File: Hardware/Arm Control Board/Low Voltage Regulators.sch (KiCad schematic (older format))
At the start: 16 parts

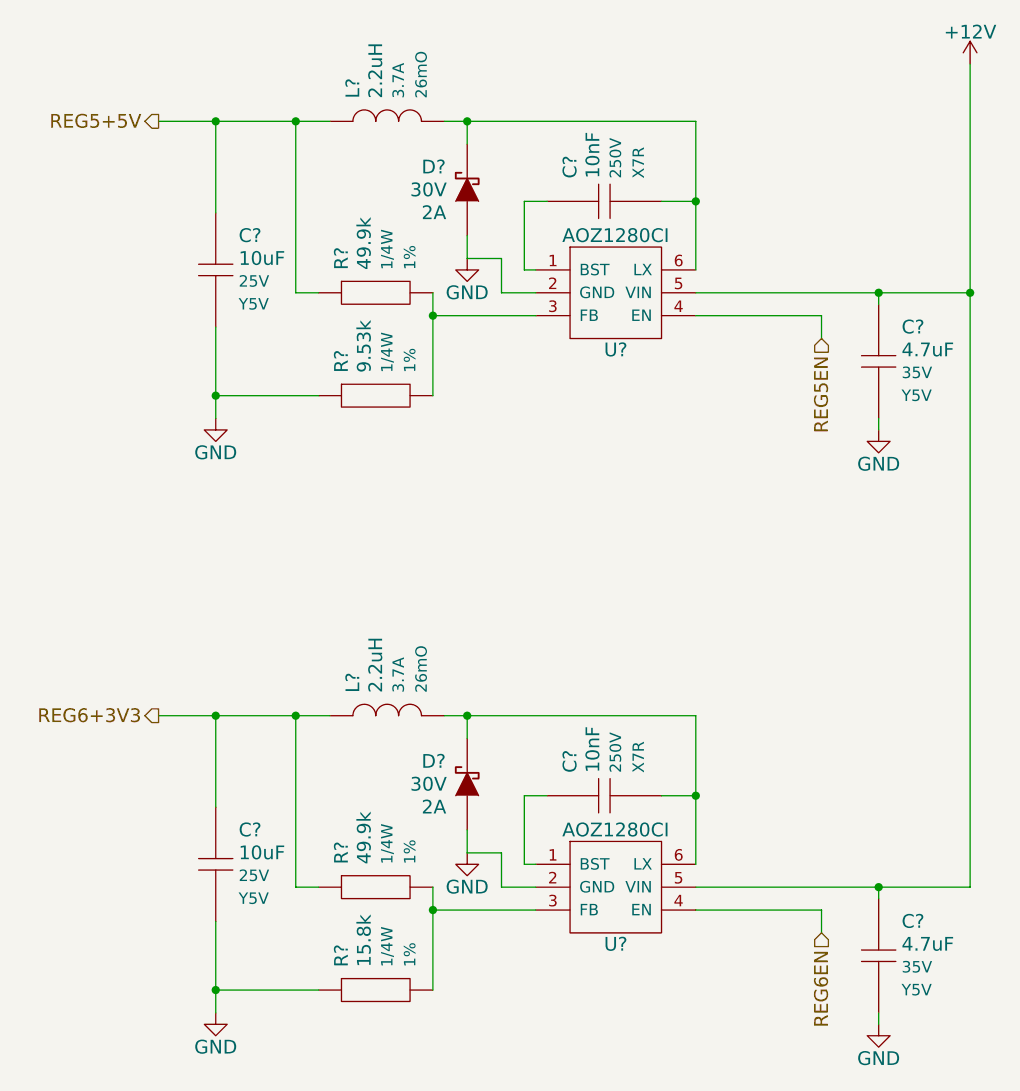
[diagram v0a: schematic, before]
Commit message: More footprints added, components annotated
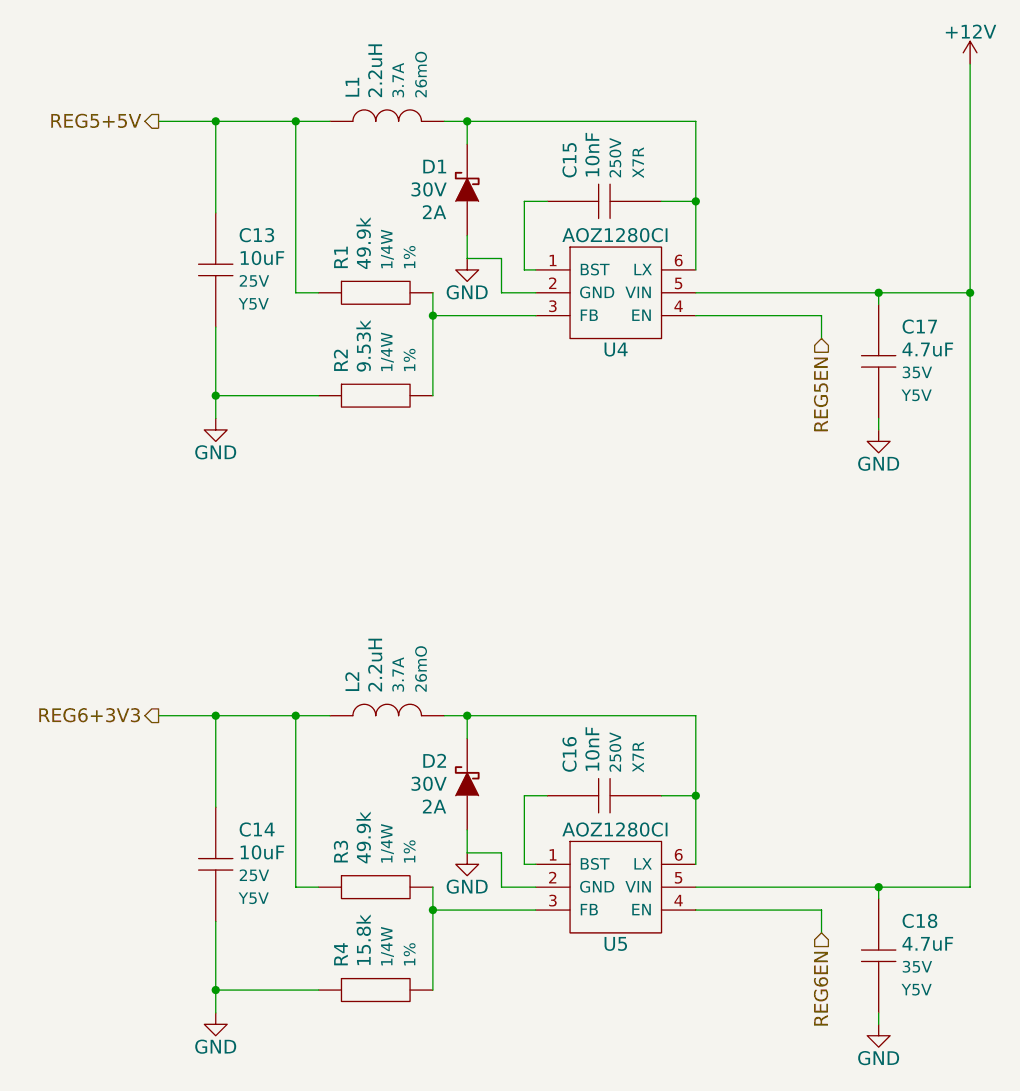
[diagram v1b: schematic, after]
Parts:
- gave numbers to parts that had none: 16
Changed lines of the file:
@@
 $EndDescr
 $Comp
-L AOZ1280CI U?
+L AOZ1280CI U5
 U 1 1 54CCFE02
 P 4200 5050
-F 0 "U?" H 4000 4700 60  0000 C CNN
+F 0 "U5" H 4000 4700 60  0000 C CNN
 F 1 "AOZ1280CI" H 4000 5200 60  0000 C CNN
 F 2 "" H 4200 5050 60  0000 C CNN
@@
 	5550 5150 4350 5150
 $Comp
-L GND #PWR?
+L GND #PWR28
 U 1 1 54CCFE12
 P 5150 5750
-F 0 "#PWR?" H 5150 5500 60  0001 C CNN
+F 0 "#PWR28" H 5150 5500 60  0001 C CNN
 F 1 "GND" H 5150 5600 60  0000 C CNN
 F 2 "" H 5150 5750 60  0000 C CNN
@@
 	2600 5150 2700 5150
 $Comp
-L DIODESCH D?
+L DIODESCH D2
 U 1 1 54CCFE3A
 P 3350 4700
-F 0 "D?" V 3450 4900 60  0000 R CNN
+F 0 "D2" V 3450 4900 60  0000 R CNN
 F 1 "DIODESCH" H 3250 5050 50  0001 C CNN
 F 2 "" H 3350 4700 60  0000 C CNN
@@
 $EndComp
 $Comp
-L GND #PWR?
+L GND #PWR24
 U 1 1 54CCFE41
 P 2250 5700
-F 0 "#PWR?" H 2250 5450 60  0001 C CNN
+F 0 "#PWR24" H 2250 5450 60  0001 C CNN
 F 1 "GND" H 2250 5550 60  0000 C CNN
 F 2 "" H 2250 5700 60  0000 C CNN
@@
 	3350 5000 3350 4900
 $Comp
-L GND #PWR?
+L GND #PWR26
 U 1 1 54CCFE56
 P 3350 5000
-F 0 "#PWR?" H 3350 4750 60  0001 C CNN
+F 0 "#PWR26" H 3350 4750 60  0001 C CNN
 F 1 "GND" H 3350 4850 60  0000 C CNN
 F 2 "" H 3350 5000 60  0000 C CNN
@@
 Connection ~ 5150 5150
 $Comp
-L Capacitor C?
+L Capacitor C14
 U 1 1 54CE875A
 P 2250 5050
-F 0 "C?" V 2100 5150 60  0000 L CNN
+F 0 "C14" V 2100 5150 60  0000 L CNN
 F 1 "10uF" V 2200 5150 60  0000 L CNN
 F 2 "Capacitors_SMD:C_1206_HandSoldering" H 2150 5050 60  0001 C CNN
@@
 $EndComp
 $Comp
-L Capacitor C?
+L Capacitor C18
 U 1 1 54CEAD10
 P 5150 5450
-F 0 "C?" V 5000 5550 60  0000 L CNN
+F 0 "C18" V 5000 5550 60  0000 L CNN
 F 1 "4.7uF" V 5100 5550 60  0000 L CNN
 F 2 "Capacitors_SMD:C_1206_HandSoldering" H 5050 5450 60  0001 C CNN
@@
 	5150 5700 5150 5750
 $Comp
-L Capacitor C?
+L Capacitor C16
 U 1 1 54CEB334
 P 3950 4750
-F 0 "C?" V 3800 4850 60  0000 L CNN
+F 0 "C16" V 3800 4850 60  0000 L CNN
 F 1 "10nF" V 3900 4850 60  0000 L CNN
 F 2 "Capacitors_SMD:C_1206_HandSoldering" H 3850 4750 60  0001 C CNN
@@
 Connection ~ 2600 4400
 $Comp
-L Inductor L?
+L Inductor L2
 U 1 1 54CEB603
 P 3000 4400
-F 0 "L?" V 2850 4500 60  0000 L CNN
+F 0 "L2" V 2850 4500 60  0000 L CNN
 F 1 "2.2uH" V 2950 4500 60  0000 L CNN
 F 2 "" H 2900 4400 60  0001 C CNN
@@
 $EndComp
 $Comp
-L Resistor R?
+L Resistor R3
 U 1 1 54CEC508
 P 2950 5150
-F 0 "R?" V 2800 5250 60  0000 L CNN
+F 0 "R3" V 2800 5250 60  0000 L CNN
 F 1 "49.9k" V 2900 5250 60  0000 L CNN
 F 2 "Resistors_SMD:R_1206_HandSoldering" H 2850 5150 60  0001 C CNN
@@
 $EndComp
 $Comp
-L Resistor R?
+L Resistor R4
 U 1 1 54CEC68A
 P 2950 5600
-F 0 "R?" V 2800 5700 60  0000 L CNN
+F 0 "R4" V 2800 5700 60  0000 L CNN
 F 1 "15.8k" V 2900 5700 60  0000 L CNN
 F 2 "Resistors_SMD:R_1206_HandSoldering" H 2850 5600 60  0001 C CNN
@@
 $EndComp
 $Comp
-L AOZ1280CI U?
+L AOZ1280CI U4
 U 1 1 54CED059
 P 4200 2450
-F 0 "U?" H 4000 2100 60  0000 C CNN
+F 0 "U4" H 4000 2100 60  0000 C CNN
 F 1 "AOZ1280CI" H 4000 2600 60  0000 C CNN
 F 2 "" H 4200 2450 60  0000 C CNN
@@
 	4350 2550 5550 2550
 $Comp
-L GND #PWR?
+L GND #PWR27
 U 1 1 54CED061
 P 5150 3150
-F 0 "#PWR?" H 5150 2900 60  0001 C CNN
+F 0 "#PWR27" H 5150 2900 60  0001 C CNN
 F 1 "GND" H 5150 3000 60  0000 C CNN
 F 2 "" H 5150 3150 60  0000 C CNN
@@
 	2600 2550 2700 2550
 $Comp
-L DIODESCH D?
+L DIODESCH D1
 U 1 1 54CED079
 P 3350 2100
-F 0 "D?" V 3450 2300 60  0000 R CNN
+F 0 "D1" V 3450 2300 60  0000 R CNN
 F 1 "DIODESCH" H 3250 2450 50  0001 C CNN
 F 2 "" H 3350 2100 60  0000 C CNN
@@
 $EndComp
 $Comp
-L GND #PWR?
+L GND #PWR23
 U 1 1 54CED07F
 P 2250 3100
-F 0 "#PWR?" H 2250 2850 60  0001 C CNN
+F 0 "#PWR23" H 2250 2850 60  0001 C CNN
 F 1 "GND" H 2250 2950 60  0000 C CNN
 F 2 "" H 2250 3100 60  0000 C CNN
@@
 	3350 2400 3350 2300
 $Comp
-L GND #PWR?
+L GND #PWR25
 U 1 1 54CED08E
 P 3350 2400
-F 0 "#PWR?" H 3350 2150 60  0001 C CNN
+F 0 "#PWR25" H 3350 2150 60  0001 C CNN
 F 1 "GND" H 3350 2250 60  0000 C CNN
 F 2 "" H 3350 2400 60  0000 C CNN
@@
 Connection ~ 5150 2550
 $Comp
-L Capacitor C?
+L Capacitor C13
 U 1 1 54CED0A8
 P 2250 2450
-F 0 "C?" V 2100 2550 60  0000 L CNN
+F 0 "C13" V 2100 2550 60  0000 L CNN
 F 1 "10uF" V 2200 2550 60  0000 L CNN
 F 2 "Capacitors_SMD:C_1206_HandSoldering" H 2150 2450 60  0001 C CNN
@@
 $EndComp
 $Comp
-L Capacitor C?
+L Capacitor C17
 U 1 1 54CED0B4
 P 5150 2850
-F 0 "C?" V 5000 2950 60  0000 L CNN
+F 0 "C17" V 5000 2950 60  0000 L CNN
 F 1 "4.7uF" V 5100 2950 60  0000 L CNN
 F 2 "Capacitors_SMD:C_1206_HandSoldering" H 5050 2850 60  0001 C CNN
@@
 	5150 3100 5150 3150
 $Comp
-L Capacitor C?
+L Capacitor C15
 U 1 1 54CED0C1
 P 3950 2150
-F 0 "C?" V 3800 2250 60  0000 L CNN
+F 0 "C15" V 3800 2250 60  0000 L CNN
 F 1 "10nF" V 3900 2250 60  0000 L CNN
 F 2 "Capacitors_SMD:C_1206_HandSoldering" H 3850 2150 60  0001 C CNN
@@
 Connection ~ 2600 1800
 $Comp
-L Inductor L?
+L Inductor L1
 U 1 1 54CED0CF
 P 3000 1800
-F 0 "L?" V 2850 1900 60  0000 L CNN
+F 0 "L1" V 2850 1900 60  0000 L CNN
 F 1 "2.2uH" V 2950 1900 60  0000 L CNN
 F 2 "" H 2900 1800 60  0001 C CNN
@@
 $EndComp
 $Comp
-L Resistor R?
+L Resistor R1
 U 1 1 54CED0DB
 P 2950 2550
-F 0 "R?" V 2800 2650 60  0000 L CNN
+F 0 "R1" V 2800 2650 60  0000 L CNN
 F 1 "49.9k" V 2900 2650 60  0000 L CNN
 F 2 "Resistors_SMD:R_1206_HandSoldering" H 2850 2550 60  0001 C CNN
@@
 $EndComp
 $Comp
-L Resistor R?
+L Resistor R2
 U 1 1 54CED0E7
 P 2950 3000
-F 0 "R?" V 2800 3100 60  0000 L CNN
+F 0 "R2" V 2800 3100 60  0000 L CNN
 F 1 "9.53k" V 2900 3100 60  0000 L CNN
 F 2 "Resistors_SMD:R_1206_HandSoldering" H 2850 3000 60  0001 C CNN
@@
 Connection ~ 5550 2550
 $Comp
-L +12V #PWR?
+L +12V #PWR29
 U 1 1 54CEDCB5
 P 5550 1550
-F 0 "#PWR?" H 5550 1400 60  0001 C CNN
+F 0 "#PWR29" H 5550 1400 60  0001 C CNN
 F 1 "+12V" H 5550 1690 60  0000 C CNN
 F 2 "" H 5550 1550 60  0000 C CNN

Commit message: Initial PCB layout
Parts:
- U4, U5: footprint (none) -> SMD_Packages:SOT-23-6
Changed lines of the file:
@@
 F 0 "U5" H 4000 4700 60  0000 C CNN
 F 1 "AOZ1280CI" H 4000 5200 60  0000 C CNN
-F 2 "" H 4200 5050 60  0000 C CNN
+F 2 "SMD_Packages:SOT-23-6" H 4200 5050 60  0001 C CNN
 F 3 "" H 4200 5050 60  0000 C CNN
 	1    4200 5050
@@
 	5550 5150 4350 5150
 $Comp
-L GND #PWR28
+L GND #PWR025
 U 1 1 54CCFE12
 P 5150 5750
-F 0 "#PWR28" H 5150 5500 60  0001 C CNN
+F 0 "#PWR025" H 5150 5500 60  0001 C CNN
 F 1 "GND" H 5150 5600 60  0000 C CNN
 F 2 "" H 5150 5750 60  0000 C CNN
@@
 $EndComp
 $Comp
-L GND #PWR24
+L GND #PWR026
 U 1 1 54CCFE41
 P 2250 5700
-F 0 "#PWR24" H 2250 5450 60  0001 C CNN
+F 0 "#PWR026" H 2250 5450 60  0001 C CNN
 F 1 "GND" H 2250 5550 60  0000 C CNN
 F 2 "" H 2250 5700 60  0000 C CNN
@@
 	3350 5000 3350 4900
 $Comp
-L GND #PWR26
+L GND #PWR027
 U 1 1 54CCFE56
 P 3350 5000
-F 0 "#PWR26" H 3350 4750 60  0001 C CNN
+F 0 "#PWR027" H 3350 4750 60  0001 C CNN
 F 1 "GND" H 3350 4850 60  0000 C CNN
 F 2 "" H 3350 5000 60  0000 C CNN
@@
 F 0 "U4" H 4000 2100 60  0000 C CNN
 F 1 "AOZ1280CI" H 4000 2600 60  0000 C CNN
-F 2 "" H 4200 2450 60  0000 C CNN
+F 2 "SMD_Packages:SOT-23-6" H 4200 2450 60  0001 C CNN
 F 3 "" H 4200 2450 60  0000 C CNN
 	1    4200 2450
@@
 	4350 2550 5550 2550
 $Comp
-L GND #PWR27
+L GND #PWR028
 U 1 1 54CED061
 P 5150 3150
-F 0 "#PWR27" H 5150 2900 60  0001 C CNN
+F 0 "#PWR028" H 5150 2900 60  0001 C CNN
 F 1 "GND" H 5150 3000 60  0000 C CNN
 F 2 "" H 5150 3150 60  0000 C CNN
@@
 $EndComp
 $Comp
-L GND #PWR23
+L GND #PWR029
 U 1 1 54CED07F
 P 2250 3100
-F 0 "#PWR23" H 2250 2850 60  0001 C CNN
+F 0 "#PWR029" H 2250 2850 60  0001 C CNN
 F 1 "GND" H 2250 2950 60  0000 C CNN
 F 2 "" H 2250 3100 60  0000 C CNN
@@
 	3350 2400 3350 2300
 $Comp
-L GND #PWR25
+L GND #PWR030
 U 1 1 54CED08E
 P 3350 2400
-F 0 "#PWR25" H 3350 2150 60  0001 C CNN
+F 0 "#PWR030" H 3350 2150 60  0001 C CNN
 F 1 "GND" H 3350 2250 60  0000 C CNN
 F 2 "" H 3350 2400 60  0000 C CNN
@@
 Connection ~ 5550 2550
 $Comp
-L +12V #PWR29
+L +12V #PWR031
 U 1 1 54CEDCB5
 P 5550 1550
-F 0 "#PWR29" H 5550 1400 60  0001 C CNN
+F 0 "#PWR031" H 5550 1400 60  0001 C CNN
 F 1 "+12V" H 5550 1690 60  0000 C CNN
 F 2 "" H 5550 1550 60  0000 C CNN

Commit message: all components have footprints assigned now
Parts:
- D1, D2: footprint (none) -> MAVRIC_footprints:Diode_MicroSMP
- L1, L2: footprint (none) -> MAVRIC_footprints:Yuden_SMD_Power_Inductor_6060
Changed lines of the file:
@@
 F 0 "D2" V 3450 4900 60  0000 R CNN
 F 1 "DIODESCH" H 3250 5050 50  0001 C CNN
-F 2 "" H 3350 4700 60  0000 C CNN
+F 2 "MAVRIC_footprints:Diode_MicroSMP" H 3350 4700 60  0001 C CNN
 F 3 "" H 3350 4700 60  0000 C CNN
 F 4 "Vishay Semiconductor" H 3350 4700 60  0001 C CNN "Manufacturer"
@@
 F 0 "L2" V 2850 4500 60  0000 L CNN
 F 1 "2.2uH" V 2950 4500 60  0000 L CNN
-F 2 "" H 2900 4400 60  0001 C CNN
+F 2 "MAVRIC_footprints:Yuden_SMD_Power_Inductor_6060" H 2900 4400 60  0001 C CNN
 F 3 "" H 3000 4500 60  0001 C CNN
 F 4 "Taiyo Yuden" H 3000 4400 60  0001 C CNN "Manufacturer"
@@
 F 0 "D1" V 3450 2300 60  0000 R CNN
 F 1 "DIODESCH" H 3250 2450 50  0001 C CNN
-F 2 "" H 3350 2100 60  0000 C CNN
+F 2 "MAVRIC_footprints:Diode_MicroSMP" H 3350 2100 60  0001 C CNN
 F 3 "" H 3350 2100 60  0000 C CNN
 F 4 "Vishay Semiconductor" H 3350 2100 60  0001 C CNN "Manufacturer"
@@
 F 0 "L1" V 2850 1900 60  0000 L CNN
 F 1 "2.2uH" V 2950 1900 60  0000 L CNN
-F 2 "" H 2900 1800 60  0001 C CNN
+F 2 "MAVRIC_footprints:Yuden_SMD_Power_Inductor_6060" H 2900 1800 60  0001 C CNN
 F 3 "" H 3000 1900 60  0001 C CNN
 F 4 "Taiyo Yuden" H 3000 1800 60  0001 C CNN "Manufacturer"
